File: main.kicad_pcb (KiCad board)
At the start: 2 copper layers, 100 x 80 mm, 45 parts

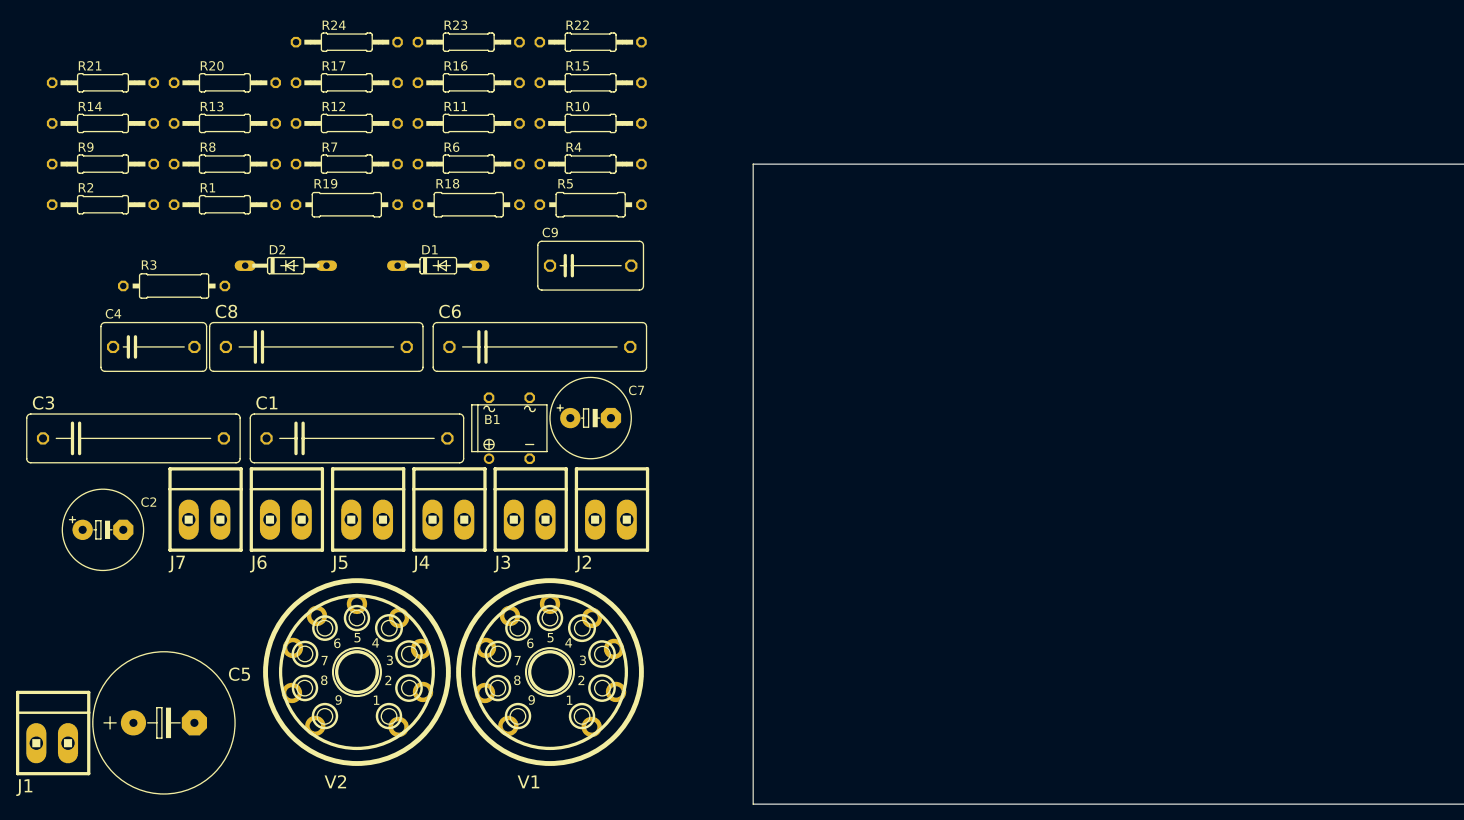
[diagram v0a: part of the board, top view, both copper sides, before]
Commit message: Renamed footprints in libs to deal with error of importing to pcbdoc
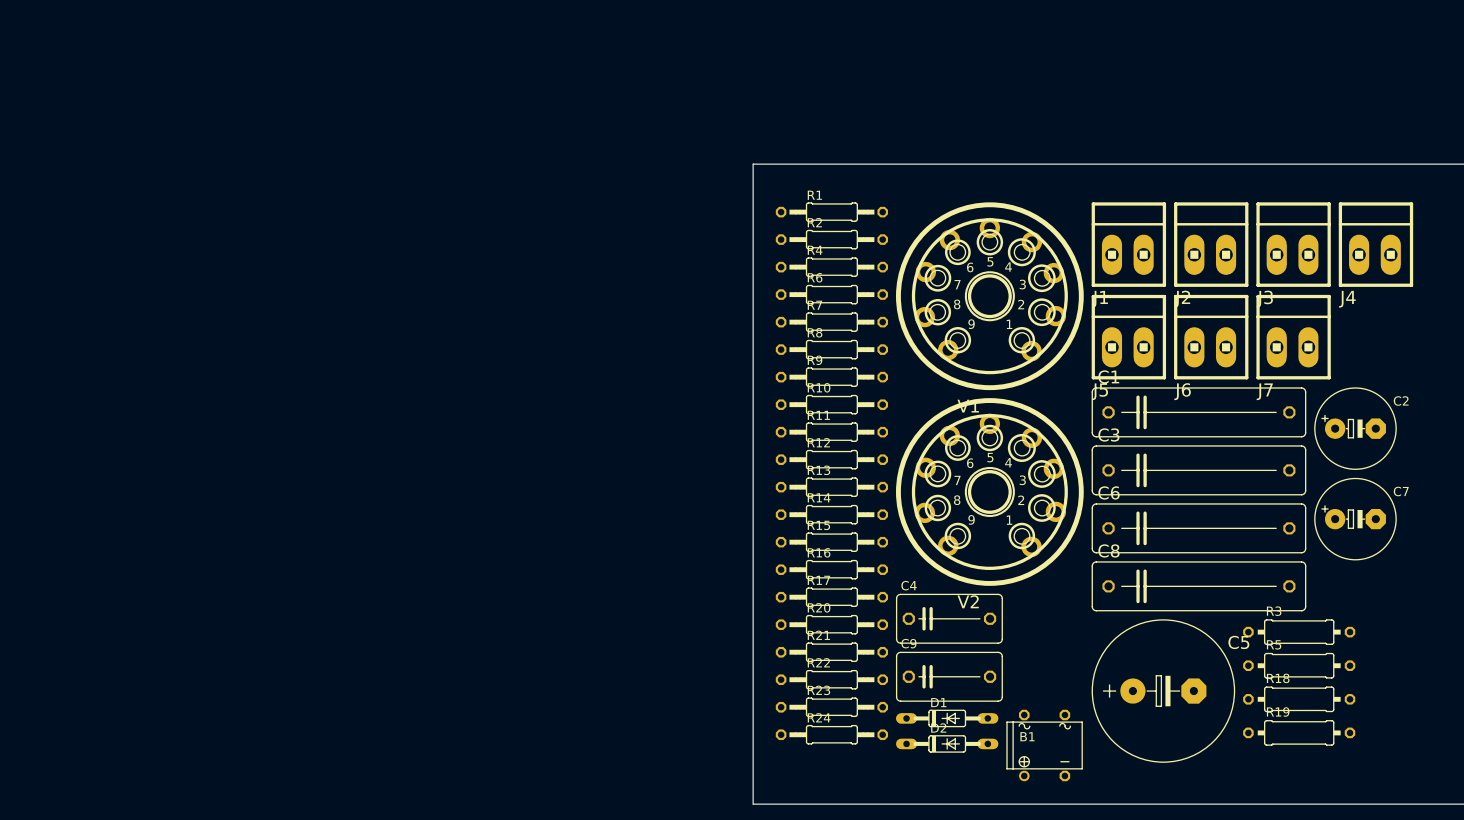
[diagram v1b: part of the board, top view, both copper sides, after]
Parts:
- B1: value (none) -> B-DIL; footprint main:B-DIL_336 -> main:B-DIL
- C1, C3, C6, C8: value 1u -> C-EU225-062X268; footprint main:C225-062X268_334 -> main:C225-062X268
- C2, C7: value 330u 35V -> CPOL-EUE5-10.5; footprint main:E5-10,5_334 -> main:E5-10,5
- C4, C9: value 22n -> C-EU102-064X133; footprint main:C102-064X133_334 -> main:C102-064X133
- C5: value 100u 350V -> CPOL-EUE7.5-18; footprint main:E7,5-18_334 -> main:E7,5-18
- D1, D2: footprint main:DO35-10_210 -> main:DO35-10
- J1, J2, J3, J4, J5, J6, J7: value (none) -> MTA02-156; footprint main:1X2MTA_127 -> main:1X2MTA
- R1, R16, R22, R8: value 1M -> R-EU_0207/12; footprint main:0207_12_334 -> main:0207_12
- R10, R24: value 3k9 -> R-EU_0207/12; footprint main:0207_12_334 -> main:0207_12
- R11, R12, R13, R14: value 660 -> R-EU_0207/12; footprint main:0207_12_334 -> main:0207_12
- R15, R2, R23, R9: value 10k -> R-EU_0207/12; footprint main:0207_12_334 -> main:0207_12
- R17, R4: value 220 -> R-EU_0207/12; footprint main:0207_12_334 -> main:0207_12
- R18, R19, R3, R5: value 240k -> R-EU_0309/12; footprint main:0309_12_334 -> main:0309_12
- R20, R6: value 1k -> R-EU_0207/12; footprint main:0207_12_334 -> main:0207_12
- R21, R7: value 51k -> R-EU_0207/12; footprint main:0207_12_334 -> main:0207_12
- V1, V2: value (none) -> 12AX7-P; footprint main:NOVAL -> main:TUBE
- moved C2 157.1 mm to (173.8, 98.1)
- moved J1 147.7 mm to (145.3, 76.3)
- moved R3 147.1 mm to (166.8, 123.5)
- moved J7 137.7 mm to (165.9, 87.9)
- moved R19 136.1 mm to (166.8, 136.1)
- moved C3 133.2 mm to (154.2, 103.3)
- moved C5 125.0 mm to (149.8, 130.9)
- moved R18 120.8 mm to (166.8, 131.9)
- moved J4 120.5 mm to (176.2, 76.3)
- moved J6 117.5 mm to (155.6, 87.9)
- moved R21 115.6 mm to (108.3, 126.0)
- moved C8 114.3 mm to (154.2, 117.8)
- moved R24 105.7 mm to (108.3, 136.3)
- moved R5 105.7 mm to (166.8, 127.7)
- moved C1 105.3 mm to (154.2, 96.0)
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
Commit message: Made very specific edge cuts form
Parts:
- moved R8 494.7 mm to (591.4, -18.1), turned to 180 degrees
- moved D1 488.7 mm to (591.4, -4.12)
- moved R7 484.9 mm to (587.6, 11.1)
- moved R1 483.8 mm to (587.6, 4.77)
- moved C4 470.4 mm to (573.7, -13.0), turned to 90 degrees
- moved C7 468.5 mm to (632.2, 12.7)
- moved B1 456.3 mm to (585.1, 63.2)
- moved R16 452.8 mm to (545.7, -1.58), turned to 180 degrees
- moved J1 450.5 mm to (582.5, -32.1)
- moved J3 450.2 mm to (616.1, 70.8)
- moved R21 447.5 mm to (548.3, 44.1)
- moved C1 444.1 mm to (590.7, 14.2)
- moved C2 444.1 mm to (610.3, 16.2)
- moved J7 444.1 mm to (602.4, 6.04)
- moved R17 439.5 mm to (527.9, -11.7), turned to 180 degrees
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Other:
- board size 100 x 80 mm -> 160 x 80 mm

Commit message: Almost all, one connection left
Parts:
- moved J3 511.5 mm to (106.7, 116.8), turned to -90 degrees
- moved J7 490.8 mm to (113.7, 50.8), turned to 180 degrees
- moved D1 468.3 mm to (134.6, 99.1)
- moved R8 467.9 mm to (137.2, 94.0)
- moved B1 466.3 mm to (121.9, 116.8), turned to 90 degrees
- moved C4 462.4 mm to (124.5, 96.5)
- moved R7 447.1 mm to (147.3, 88.9), turned to -90 degrees
- moved J4 430.7 mm to (121.4, 71.1), turned to 180 degrees
- moved C7 430.3 mm to (208.3, 86.4)
- moved C2 429.8 mm to (182.9, 61.0)
- moved J1 428.1 mm to (162.6, 50.8), turned to 180 degrees
- moved R9 420.1 mm to (111.8, 101.6)
- moved C8 416.0 mm to (139.7, 76.2), turned to 180 degrees
- moved R21 414.5 mm to (134.6, 71.1), turned to 180 degrees
- moved C1 409.5 mm to (182.9, 50.8)
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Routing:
- net GND: track 0.00 -> 513.5 mm
- net Net-(B1-Pad+): track 0.00 -> 171.4 mm
- net Net-(V1B-TA): track 0.00 -> 85.9 mm
- net Net-(V1A-TA): track 0.00 -> 71.7 mm
- net Net-(C3-Pad1): track 0.00 -> 61.9 mm
- net Net-(C9-Pad1): track 0.00 -> 52.1 mm
- net Net-(C6-Pad2): track 0.00 -> 45.8 mm
- net Net-(V1A-TK): track 0.00 -> 41.5 mm
- net Net-(V1C-H1): track 0.00 -> 38.6 mm
- net Net-(C1-Pad2): track 0.00 -> 30.4 mm
- net Net-(V2B-TA): track 0.00 -> 28.1 mm
- net Net-(V2C-H1): track 0.00 -> 26.7 mm
- net Net-(C3-Pad2): track 0.00 -> 24.3 mm
- net Net-(V1B-TK): track 0.00 -> 23.3 mm
- net Net-(C8-Pad2): track 0.00 -> 23.0 mm
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
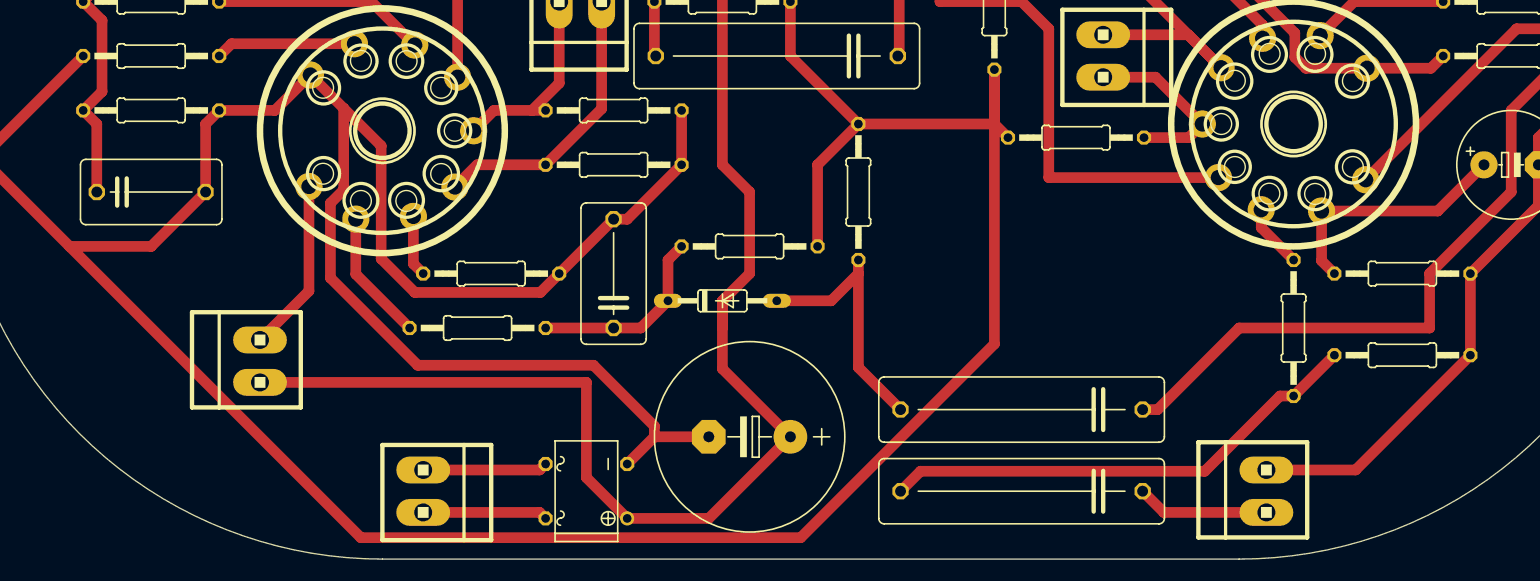
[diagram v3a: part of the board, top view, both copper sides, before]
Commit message: All parts interconnected! Only one layer used
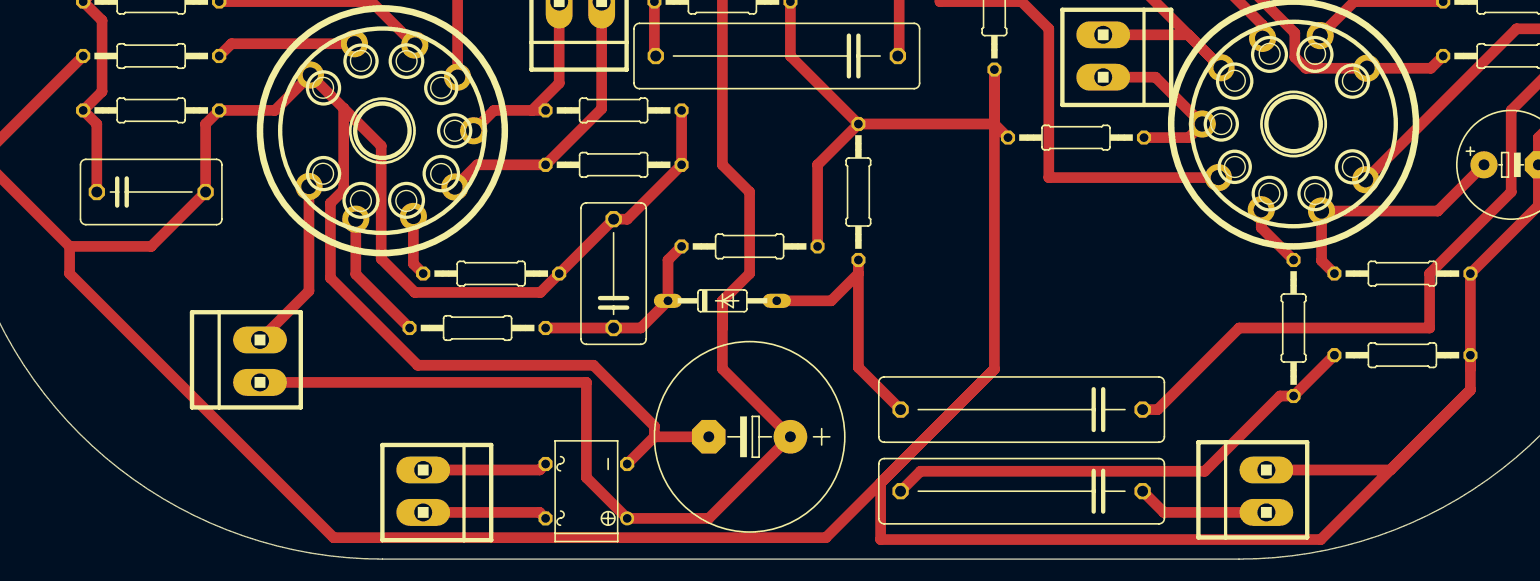
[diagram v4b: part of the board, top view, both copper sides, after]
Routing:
- net GND: track 513.5 -> 600.8 mm
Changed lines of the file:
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@@
 	)
 	(footprint "main:E7,5-18"
+		(locked yes)
 		(layer "F.Cu")
 		(at 137.16 111.76 180)
@@
 	)
 	(segment
+		(start 204.47 107.383726)
+		(end 204.47 104.14)
+		(width 1)
+		(layer "F.Cu")
+		(net 1)
+	)
+	(segment
+		(start 190.5 121.353726)
+		(end 204.47 107.383726)
+		(width 1)
+		(layer "F.Cu")
+		(net 1)
+	)
+	(segment
+		(start 196.994926 114.8588)
+		(end 204.47 107.383726)
+		(width 1)
+		(layer "F.Cu")
+		(net 1)
+	)
+	(segment
 		(start 154.94 49.53)
 		(end 159.3088 49.53)
@@
 	)
 	(segment
-		(start 119.38 96.52)
-		(end 124.46 91.44)
+		(start 149.395 121.353726)
+		(end 190.5 121.353726)
 		(width 1)
 		(layer "F.Cu")
@@
 	(segment
 		(start 119.38 96.52)
-		(end 117.6196 98.2804)
+		(end 124.46 91.44)
 		(width 1)
 		(layer "F.Cu")
@@
 	)
 	(segment
-		(start 193.7512 114.8588)
-		(end 204.47 104.14)
+		(start 119.38 96.52)
+		(end 117.6196 98.2804)
 		(width 1)
 		(layer "F.Cu")
@@
 	)
 	(segment
+		(start 204.47 105.41)
+		(end 204.47 104.14)
+		(width 1)
+		(layer "F.Cu")
+		(net 1)
+	)
+	(segment
+		(start 185.42 114.8588)
+		(end 196.994926 114.8588)
+		(width 1)
+		(layer "F.Cu")
+		(net 1)
+	)
+	(segment
 		(start 98.016 89.944)
 		(end 99.253 88.707)
@@
 	)
 	(segment
-		(start 100.8585 121.1785)
-		(end 73.66 93.98)
+		(start 160.02 105.443734)
+		(end 144.285234 121.1785)
+		(width 1)
+		(layer "F.Cu")
+		(net 1)
+	)
+	(segment
+		(start 160.02 77.47)
+		(end 160.02 105.443734)
 		(width 1)
 		(layer "F.Cu")
@@
 	)
 	(segment
+		(start 149.395 116.068734)
+		(end 149.395 121.353726)
+		(width 1)
+		(layer "F.Cu")
+		(net 1)
+	)
+	(segment
 		(start 81.28 93.98)
 		(end 73.66 93.98)
@@
 	)
 	(segment
-		(start 160.02 77.47)
-		(end 160.02 103.090266)
-		(width 1)
-		(layer "F.Cu")
-		(net 1)
-	)
-	(segment
 		(start 98.016 96.924)
 		(end 98.016 89.944)
@@
 	)
 	(segment
-		(start 160.02 103.090266)
-		(end 141.931766 121.1785)
+		(start 98.3185 121.1785)
+		(end 73.66 96.52)
 		(width 1)
 		(layer "F.Cu")
@@
 	)
 	(segment
+		(start 144.285234 121.1785)
+		(end 98.3185 121.1785)
+		(width 1)
+		(layer "F.Cu")
+		(net 1)
+	)
+	(segment
 		(start 99.253 88.707)
 		(end 99.253 81.087)
@@
 	)
 	(segment
-		(start 140.97 71.12)
-		(end 140.97 76.2)
+		(start 160.02 105.443734)
+		(end 149.395 116.068734)
 		(width 1)
 		(layer "F.Cu")
@@
 	)
 	(segment
-		(start 141.931766 121.1785)
-		(end 100.8585 121.1785)
+		(start 140.97 71.12)
+		(end 140.97 76.2)
 		(width 1)
 		(layer "F.Cu")
@@
 	)
 	(segment
-		(start 185.42 114.8588)
-		(end 193.7512 114.8588)
+		(start 208.788 73.66)
+		(end 214.579582 73.66)
 		(width 1)
 		(layer "F.Cu")
@@
 	)
 	(segment
-		(start 208.788 73.66)
-		(end 214.579582 73.66)
+		(start 73.66 96.52)
+		(end 73.66 93.98)
 		(width 1)
 		(layer "F.Cu")

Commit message: Trying to fix some DRC errors
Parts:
- moved J2 5.08 mm to (96.5, 104.7)
- moved B1 2.54 mm to (121.9, 114.3)
- moved J3 2.54 mm to (106.7, 114.3)
- moved J6 1.80 mm to (184.2, 115.6)
- moved J5 1.46 mm to (168.9, 75.5)
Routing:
- net GND: track 600.8 -> 573.6 mm
- net Net-(B1-Pad+): track 171.4 -> 168.0 mm
- net Net-(V1C-H3): track 17.0 -> 14.4 mm
- net Net-(C6-Pad1): track 12.4 -> 10.6 mm
- net Net-(V2A-TA): track 16.2 -> 14.5 mm
- net Net-(C8-Pad2): track 23.0 -> 24.5 mm
- net Net-(V1B-TA): track 85.9 -> 87.3 mm
- net Net-(V1A-TA): track 71.7 -> 72.7 mm
- net Net-(V2C-H3): track 18.7 -> 18.2 mm
- net Net-(C3-Pad2): track 24.3 -> 24.8 mm

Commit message: Исправления от Димы Орлова
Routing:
- net GND: track 573.6 -> 603.1 mm
- net Net-(C9-Pad1): track 52.1 -> 67.5 mm
- net Net-(C3-Pad1): track 61.9 -> 58.2 mm
- net Net-(V1A-TA): track 72.7 -> 75.7 mm
- net Net-(B1-Pad+): track 168.0 -> 165.9 mm
- net Net-(V1B-TA): track 87.3 -> 88.1 mm
- net Net-(C1-Pad2): track 30.4 -> 31.1 mm
- net Net-(V2C-H1): track 26.7 -> 27.5 mm

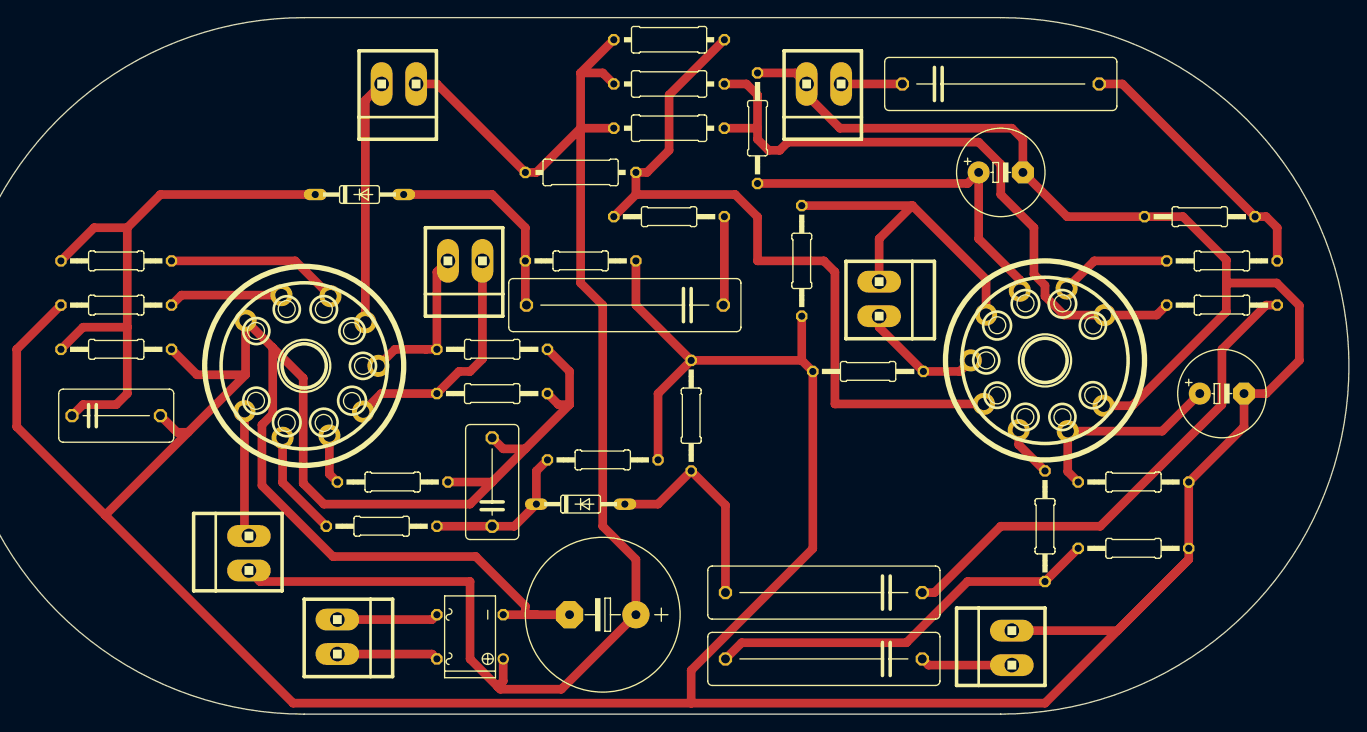
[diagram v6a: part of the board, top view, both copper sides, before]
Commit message: Диаметры у монтажных отверстий посадочных мест, -проходные дорожки
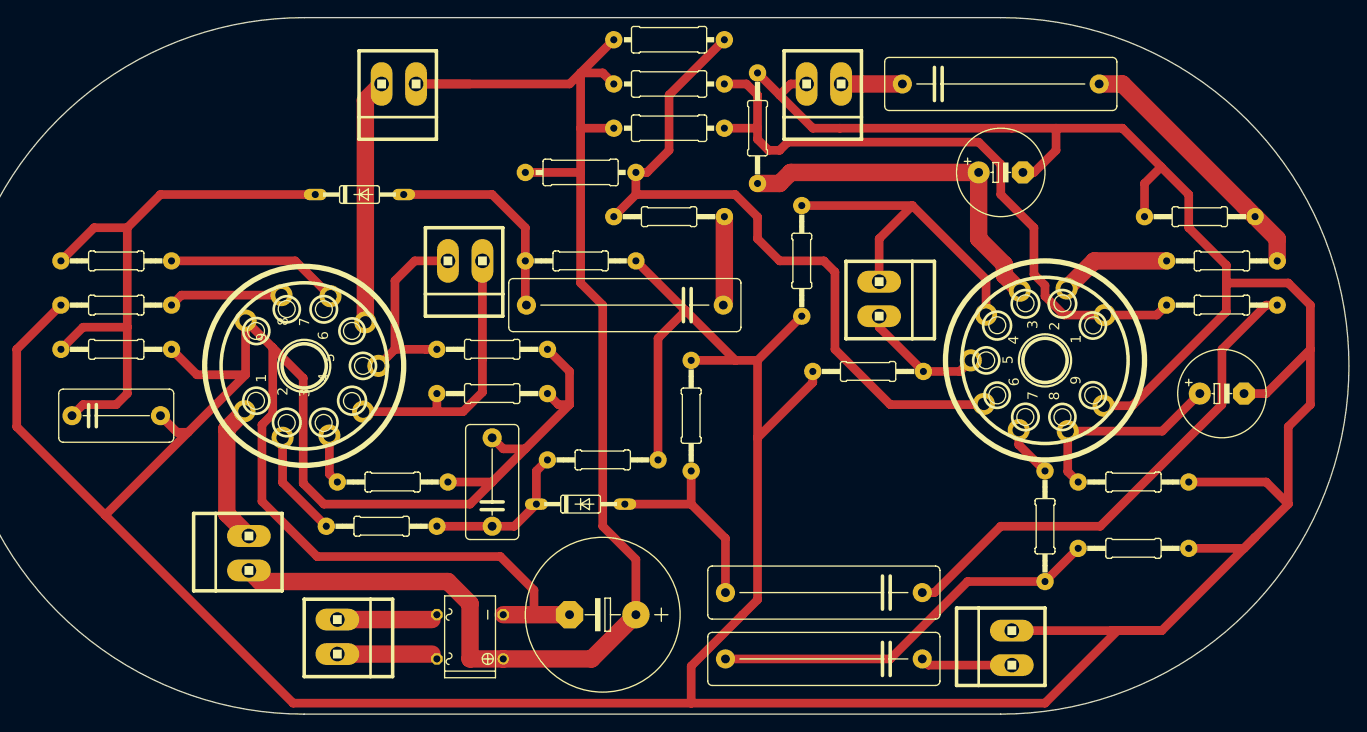
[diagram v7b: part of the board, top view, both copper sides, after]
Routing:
- net GND: track 603.1 -> 662.2 mm
- net Net-(V1B-TA): track 88.1 -> 83.0 mm
- net Net-(V2C-H1): track 27.5 -> 31.8 mm
- net Net-(V2C-H3): track 18.2 -> 22.4 mm
- net Net-(V2A-TA): track 14.5 -> 16.2 mm
- net Net-(C3-Pad2): track 24.8 -> 23.2 mm
- net Net-(B1-Pad+): track 165.9 -> 164.8 mm
- net Net-(C1-Pad2): track 31.1 -> 30.4 mm
